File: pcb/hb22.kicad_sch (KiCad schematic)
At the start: 13 parts

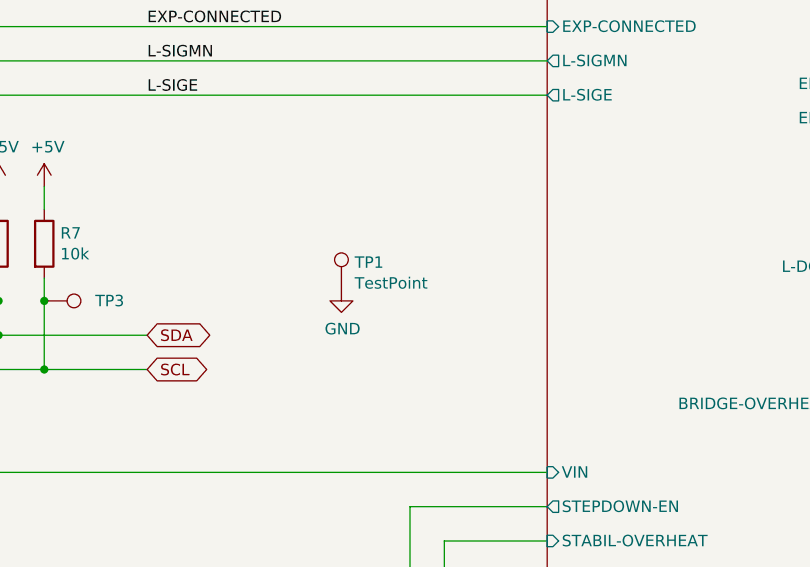
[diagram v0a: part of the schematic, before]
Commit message: Use ATmega328pb instead of ATmega328p.
Reason: obtain some free pins as a reserve.
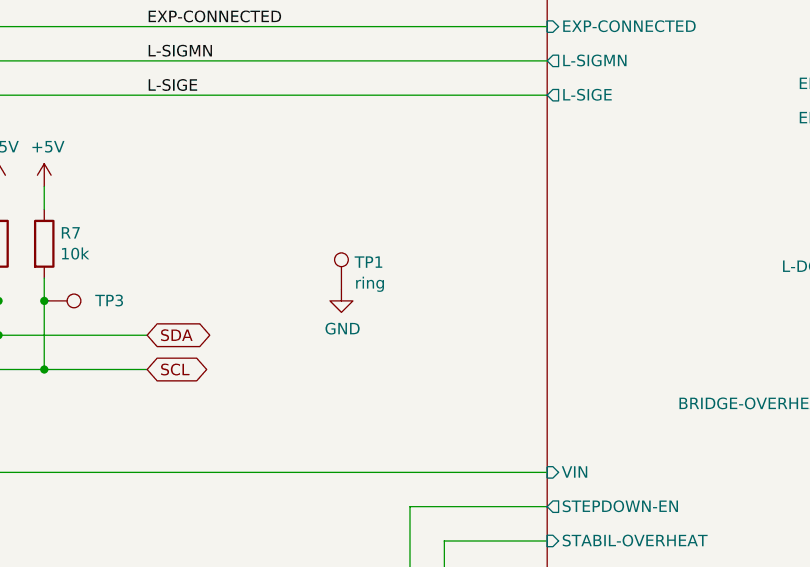
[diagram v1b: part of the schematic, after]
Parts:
- TP1: value TestPoint -> ring
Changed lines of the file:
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@@
 			)
 		)
-		(property "Value" "TestPoint"
+		(property "Value" "ring"
 			(at 103.0732 81.8642 0)
 			(effects
